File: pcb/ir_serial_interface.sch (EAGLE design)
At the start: 27 parts, among them IC1 PIC18F2550_28W, IC2 LP2992, Q2 MMBT6428LT1G, T1 PS401

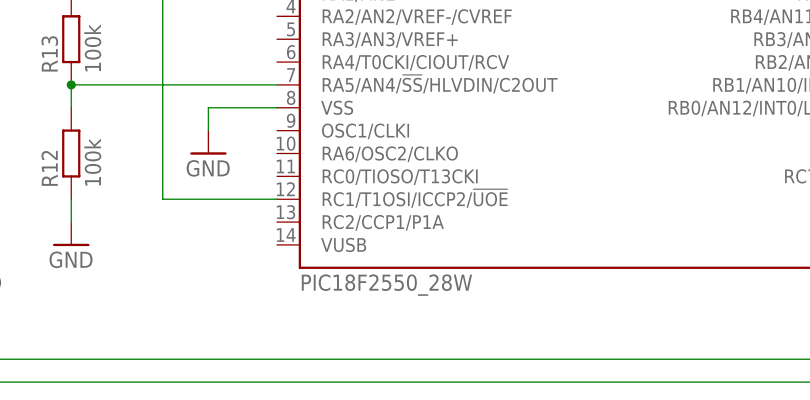
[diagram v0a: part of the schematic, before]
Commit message: PCB: silk complete
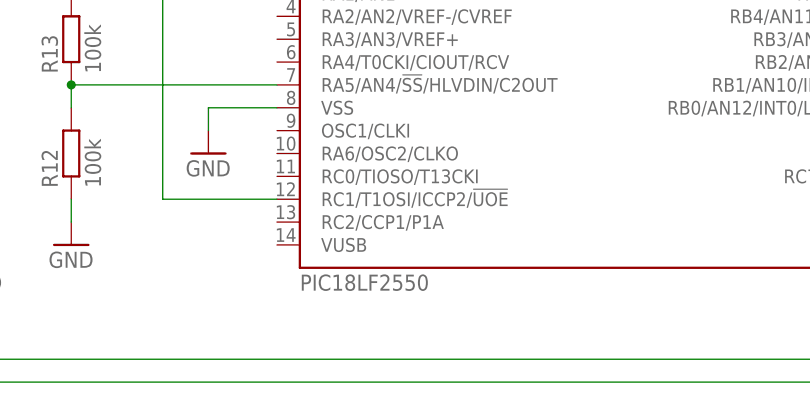
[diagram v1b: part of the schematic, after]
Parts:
- IC1: value PIC18F2550_28W -> PIC18LF2550
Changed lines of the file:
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@@
 <part name="R3" library="resistor" deviceset="R-EU_" device="M0805" value="100k"/>
 <part name="C2" library="SparkFun (old)" deviceset="CAP" device="0805" value="220nF"/>
-<part name="IC1" library="microchip" deviceset="PIC18F2*_28" device="W" technology="550"/>
+<part name="IC1" library="microchip" deviceset="PIC18F2*_28" device="W" technology="550" value="PIC18LF2550"/>
 <part name="C1" library="SparkFun (old)" deviceset="CAP" device="0805" value="47pF"/>
 <part name="P+4" library="supply1" deviceset="+5V" device=""/>

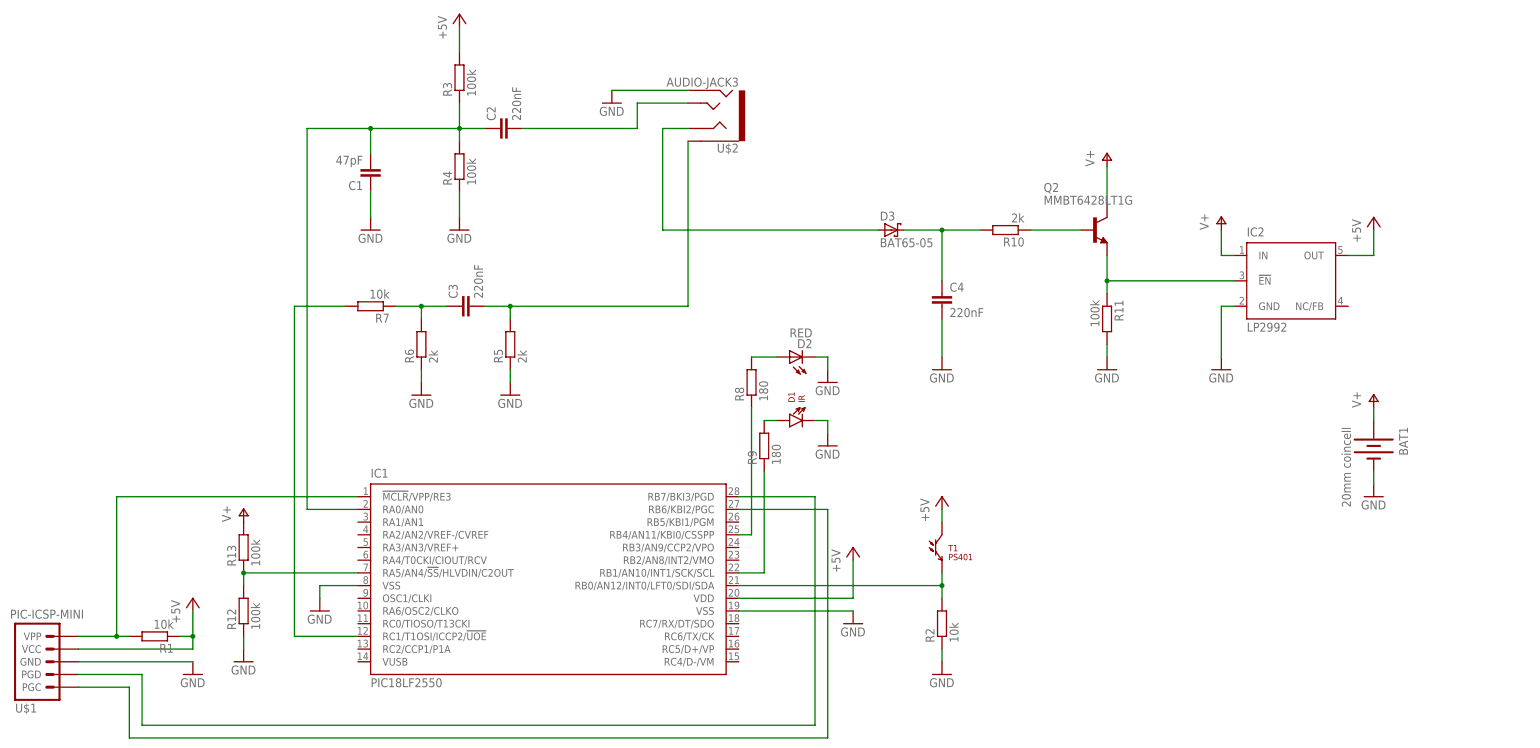
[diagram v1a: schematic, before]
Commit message: PCB: Martens rettelser
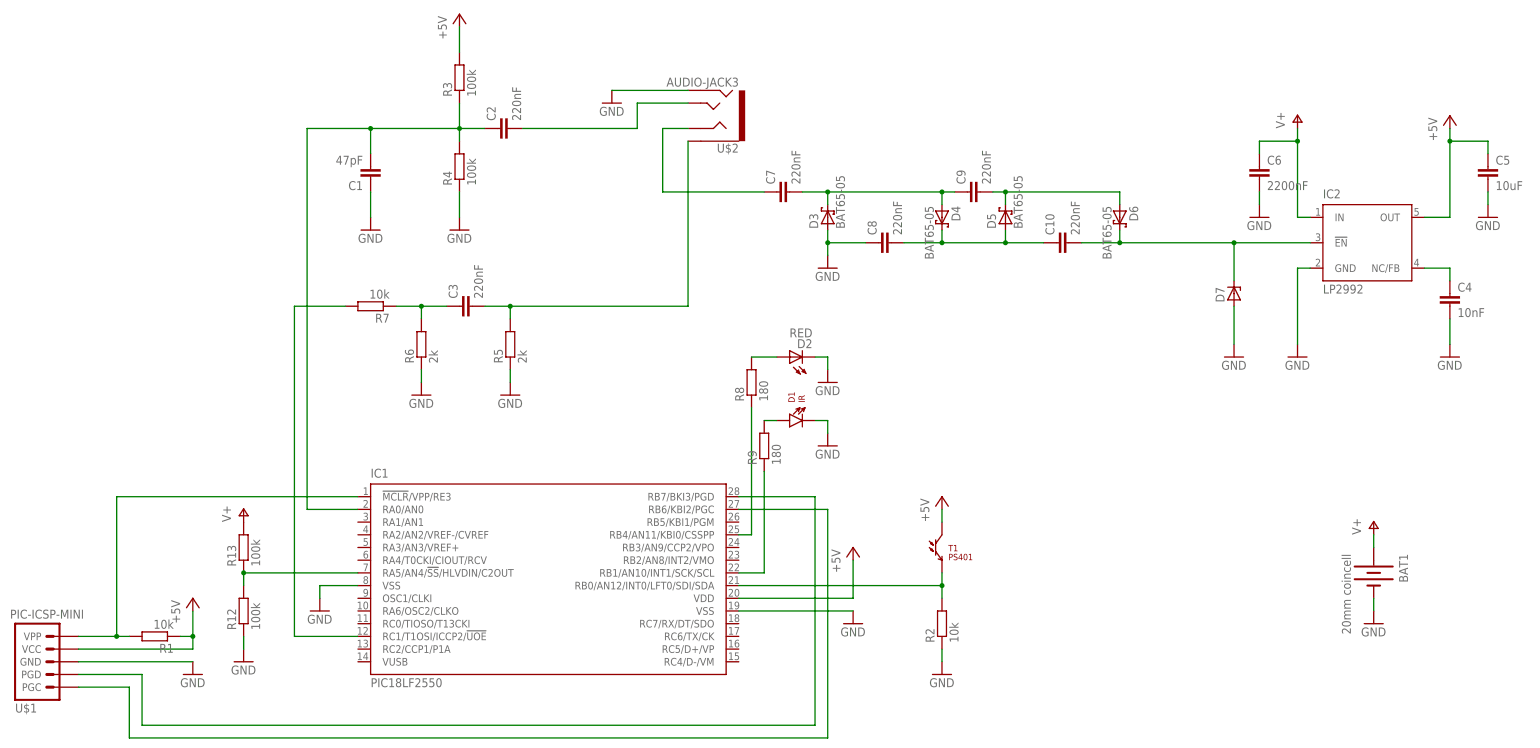
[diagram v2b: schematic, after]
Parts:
- removed Q2: MMBT6428LT1G, transistor-npn:BC847SMD
- removed R10: 2k, resistor:R-EU_M0805
- removed R11: 100k, resistor:R-EU_M0805
- added C10, C7, C8, C9: 220nF, rcl:C-EUC0805
- added C5: 10uF, rcl:C-EUC0805
- added C6: 2200nF, rcl:C-EUC0805
- added D4, D5, D6: BAT65-05, diode:BAT54
- added D7: (no value), diode:ZENER-DIODESOT23
- C4: value 220nF -> 10nF
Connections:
- new net N$21: C10.2, D6.C, D7.C, IC2.!EN
- new net N$22: C4.1, IC2.NC/FB
- net +5V: now also C5.1
- net GND: now also C5.2, C6.2, C8.1, D3.A, D7.A; no longer R11.2
- net N$12: now also C7.1; no longer D3.A
- net N$13: now also C7.2, C9.1, D3.C, D4.A; no longer IC2.!EN, Q2.E, R11.1
- net N$17: now also C9.2, D5.C, D6.A; no longer Q2.B, R10.1
- net N$18: now also C10.1, C8.2, D4.C, D5.A; no longer C4.1, D3.C, R10.2
- net V+: now also C6.1; no longer Q2.C
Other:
- moved on the sheet: BAT1, C4, D3, IC2

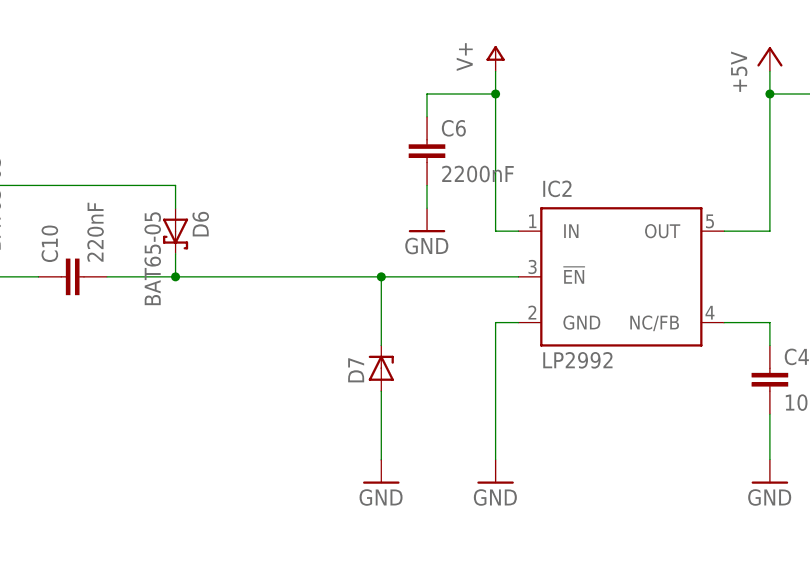
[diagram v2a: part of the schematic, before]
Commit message: PCB: missing zener
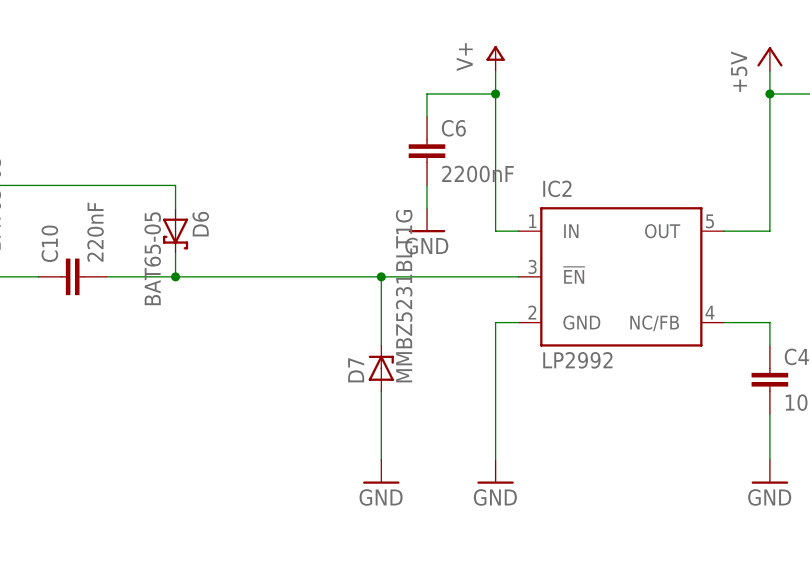
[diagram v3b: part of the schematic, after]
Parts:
- D7: value (none) -> MMBZ5231BLT1G
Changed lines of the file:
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@@
 <part name="C9" library="rcl" deviceset="C-EU" device="C0805" value="220nF"/>
 <part name="C10" library="rcl" deviceset="C-EU" device="C0805" value="220nF"/>
-<part name="D7" library="diode" deviceset="ZENER-DIODE" device="SOT23"/>
+<part name="D7" library="diode" deviceset="ZENER-DIODE" device="SOT23" value="MMBZ5231BLT1G"/>
 <part name="GND20" library="supply1" deviceset="GND" device=""/>
 </parts>

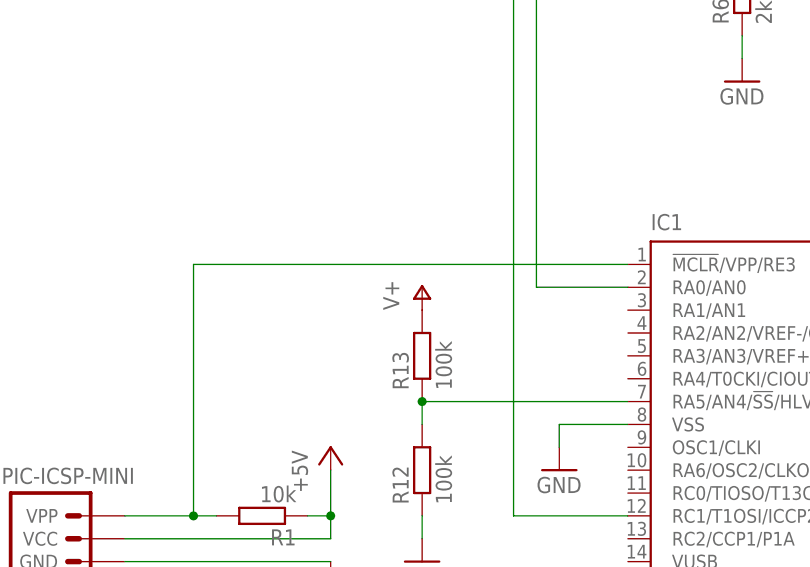
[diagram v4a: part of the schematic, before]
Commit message: PCB: fix
comparator was connected to battery/2 instead ov 5V/2
version 1.0.1
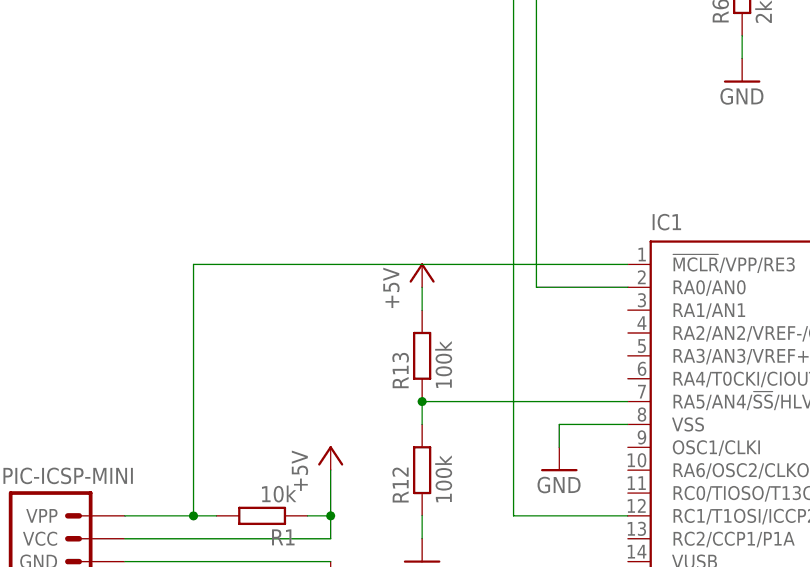
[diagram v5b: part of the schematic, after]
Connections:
- net +5V: now also R13.2
- net V+: no longer R13.2
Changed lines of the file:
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@@
 <part name="GND14" library="supply1" deviceset="GND" device=""/>
 <part name="P+7" library="supply1" deviceset="V+" device=""/>
-<part name="P+9" library="supply1" deviceset="V+" device=""/>
 <part name="GND15" library="supply1" deviceset="GND" device=""/>
 <part name="R12" library="resistor" deviceset="R-EU_" device="M0805" value="100k"/>
@@
 <part name="D7" library="diode" deviceset="ZENER-DIODE" device="SOT23" value="MMBZ5231BLT1G"/>
 <part name="GND20" library="supply1" deviceset="GND" device=""/>
+<part name="P+8" library="supply1" deviceset="+5V" device=""/>
 </parts>
 <sheets>
@@
 <instance part="GND14" gate="1" x="243.84" y="66.04"/>
 <instance part="P+7" gate="1" x="243.84" y="114.3"/>
-<instance part="P+9" gate="1" x="33.02" y="35.56"/>
 <instance part="GND15" gate="1" x="33.02" y="5.08"/>
 <instance part="R12" gate="G$1" x="33.02" y="15.24" rot="R90"/>
@@
 <instance part="D7" gate="G$1" x="231.14" y="78.74" rot="R90"/>
 <instance part="GND20" gate="1" x="231.14" y="66.04"/>
+<instance part="P+8" gate="1" x="33.02" y="38.1"/>
 </instances>
 <busses>
@@
 <wire x1="281.94" y1="109.22" x2="274.32" y2="109.22" width="0.1524" layer="91"/>
 <junction x="274.32" y="109.22"/>
+</segment>
+<segment>
+<pinref part="P+8" gate="1" pin="+5V"/>
+<pinref part="R13" gate="G$1" pin="2"/>
+<wire x1="33.02" y1="35.56" x2="33.02" y2="33.02" width="0.1524" layer="91"/>
 </segment>
 </net>
@@
 <junction x="243.84" y="109.22"/>
 </segment>
-<segment>
-<pinref part="P+9" gate="1" pin="V+"/>
-<pinref part="R13" gate="G$1" pin="2"/>
-</segment>
-</net>
+</net>

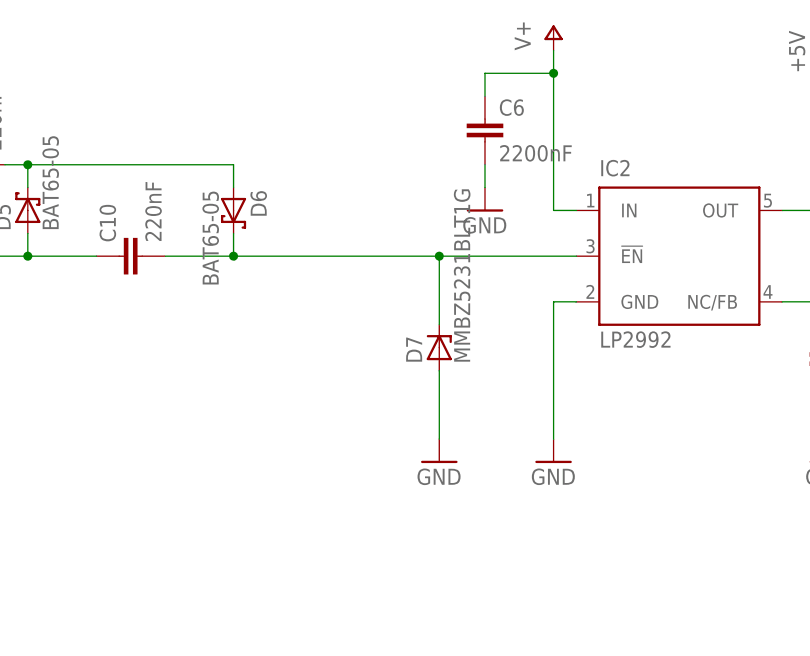
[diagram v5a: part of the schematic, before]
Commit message: PCB: no zener
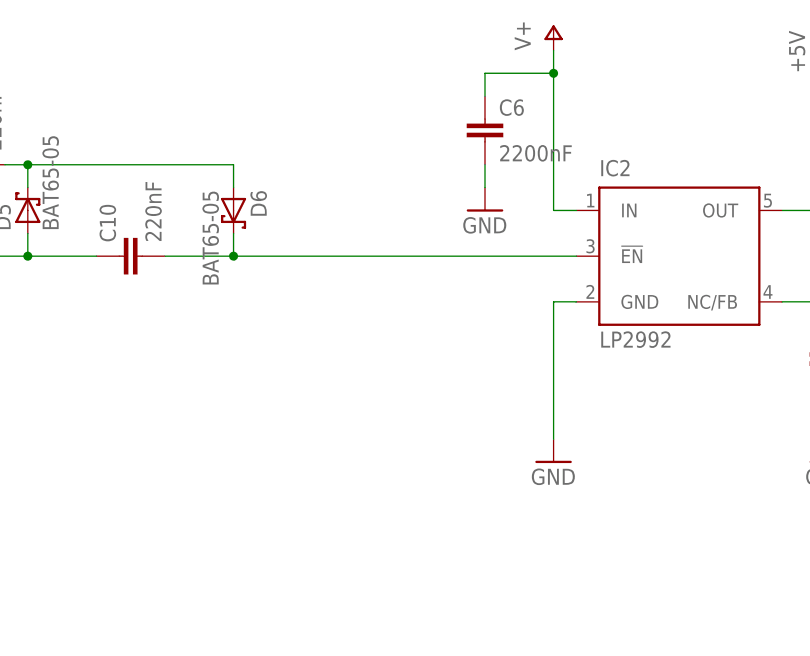
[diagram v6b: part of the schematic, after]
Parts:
- removed D7: MMBZ5231BLT1G, diode:ZENER-DIODESOT23
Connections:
- net GND: no longer D7.A
- net N$21: no longer D7.C
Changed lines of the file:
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@@
 <part name="C9" library="rcl" deviceset="C-EU" device="C0805" value="220nF"/>
 <part name="C10" library="rcl" deviceset="C-EU" device="C0805" value="220nF"/>
-<part name="D7" library="diode" deviceset="ZENER-DIODE" device="SOT23" value="MMBZ5231BLT1G"/>
-<part name="GND20" library="supply1" deviceset="GND" device=""/>
 <part name="P+8" library="supply1" deviceset="+5V" device=""/>
 </parts>
@@
 <instance part="C9" gate="G$1" x="177.8" y="99.06" rot="R90"/>
 <instance part="C10" gate="G$1" x="195.58" y="88.9" rot="R90"/>
-<instance part="D7" gate="G$1" x="231.14" y="78.74" rot="R90"/>
-<instance part="GND20" gate="1" x="231.14" y="66.04"/>
 <instance part="P+8" gate="1" x="33.02" y="38.1"/>
 </instances>
@@
 <wire x1="149.86" y1="88.9" x2="157.48" y2="88.9" width="0.1524" layer="91"/>
 <junction x="149.86" y="88.9"/>
-</segment>
-<segment>
-<pinref part="D7" gate="G$1" pin="A"/>
-<pinref part="GND20" gate="1" pin="GND"/>
-<wire x1="231.14" y1="76.2" x2="231.14" y2="68.58" width="0.1524" layer="91"/>
 </segment>
 </net>
@@
 <junction x="208.28" y="88.9"/>
 <pinref part="IC2" gate="G$1" pin="!EN"/>
-<wire x1="246.38" y1="88.9" x2="231.14" y2="88.9" width="0.1524" layer="91"/>
-<pinref part="D7" gate="G$1" pin="C"/>
-<wire x1="231.14" y1="88.9" x2="208.28" y2="88.9" width="0.1524" layer="91"/>
-<wire x1="231.14" y1="81.28" x2="231.14" y2="88.9" width="0.1524" layer="91"/>
-<junction x="231.14" y="88.9"/>
-</segment>
-</net>
+<wire x1="246.38" y1="88.9" x2="208.28" y2="88.9" width="0.1524" layer="91"/>
+</segment>
+</net>

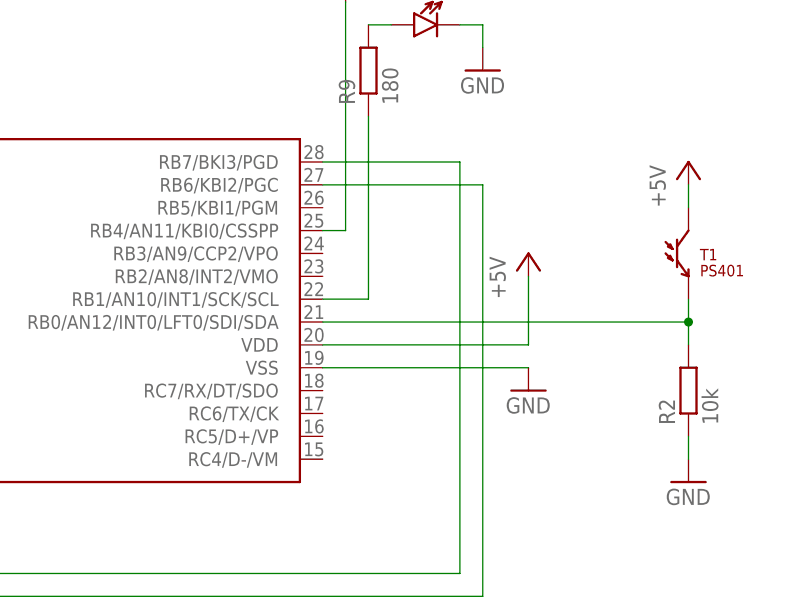
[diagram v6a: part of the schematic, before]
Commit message: PCB: reuse programmer header for serial debug
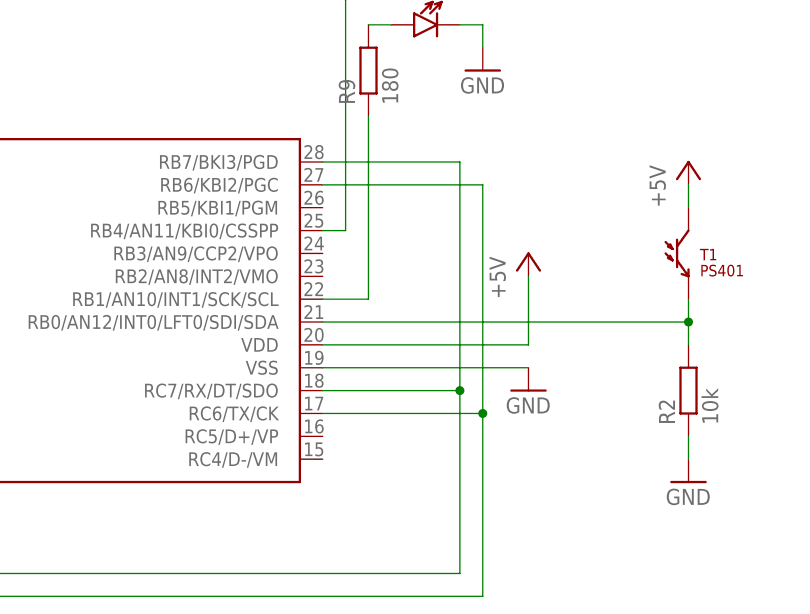
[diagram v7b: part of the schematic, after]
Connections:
- net N$3: now also IC1.RC7/RX/DT/SDO
- net N$4: now also IC1.RC6/TX/CK
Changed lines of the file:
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@@
 <wire x1="12.7" y1="2.54" x2="12.7" y2="-7.62" width="0.1524" layer="91"/>
 <wire x1="12.7" y1="-7.62" x2="147.32" y2="-7.62" width="0.1524" layer="91"/>
-<wire x1="147.32" y1="-7.62" x2="147.32" y2="38.1" width="0.1524" layer="91"/>
+<wire x1="147.32" y1="-7.62" x2="147.32" y2="12.7" width="0.1524" layer="91"/>
 <pinref part="IC1" gate="G$1" pin="RB7/BKI3/PGD"/>
+<wire x1="147.32" y1="12.7" x2="147.32" y2="38.1" width="0.1524" layer="91"/>
 <wire x1="147.32" y1="38.1" x2="132.08" y2="38.1" width="0.1524" layer="91"/>
+<pinref part="IC1" gate="G$1" pin="RC7/RX/DT/SDO"/>
+<wire x1="132.08" y1="12.7" x2="147.32" y2="12.7" width="0.1524" layer="91"/>
+<junction x="147.32" y="12.7"/>
 </segment>
 </net>
@@
 <wire x1="10.16" y1="0" x2="0" y2="0" width="0.1524" layer="91"/>
 <wire x1="10.16" y1="-10.16" x2="149.86" y2="-10.16" width="0.1524" layer="91"/>
-<wire x1="149.86" y1="-10.16" x2="149.86" y2="35.56" width="0.1524" layer="91"/>
+<wire x1="149.86" y1="-10.16" x2="149.86" y2="10.16" width="0.1524" layer="91"/>
 <pinref part="IC1" gate="G$1" pin="RB6/KBI2/PGC"/>
+<wire x1="149.86" y1="10.16" x2="149.86" y2="35.56" width="0.1524" layer="91"/>
 <wire x1="149.86" y1="35.56" x2="132.08" y2="35.56" width="0.1524" layer="91"/>
+<pinref part="IC1" gate="G$1" pin="RC6/TX/CK"/>
+<wire x1="132.08" y1="10.16" x2="149.86" y2="10.16" width="0.1524" layer="91"/>
+<junction x="149.86" y="10.16"/>
 </segment>
 </net>
